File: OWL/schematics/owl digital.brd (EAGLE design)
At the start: 60 x 56.3 mm, 59 parts, among them IC1 REG1117, IC3 IS61WV51216BLL-10TLI, U2 WM8731, U4 STM32F405ZGT6

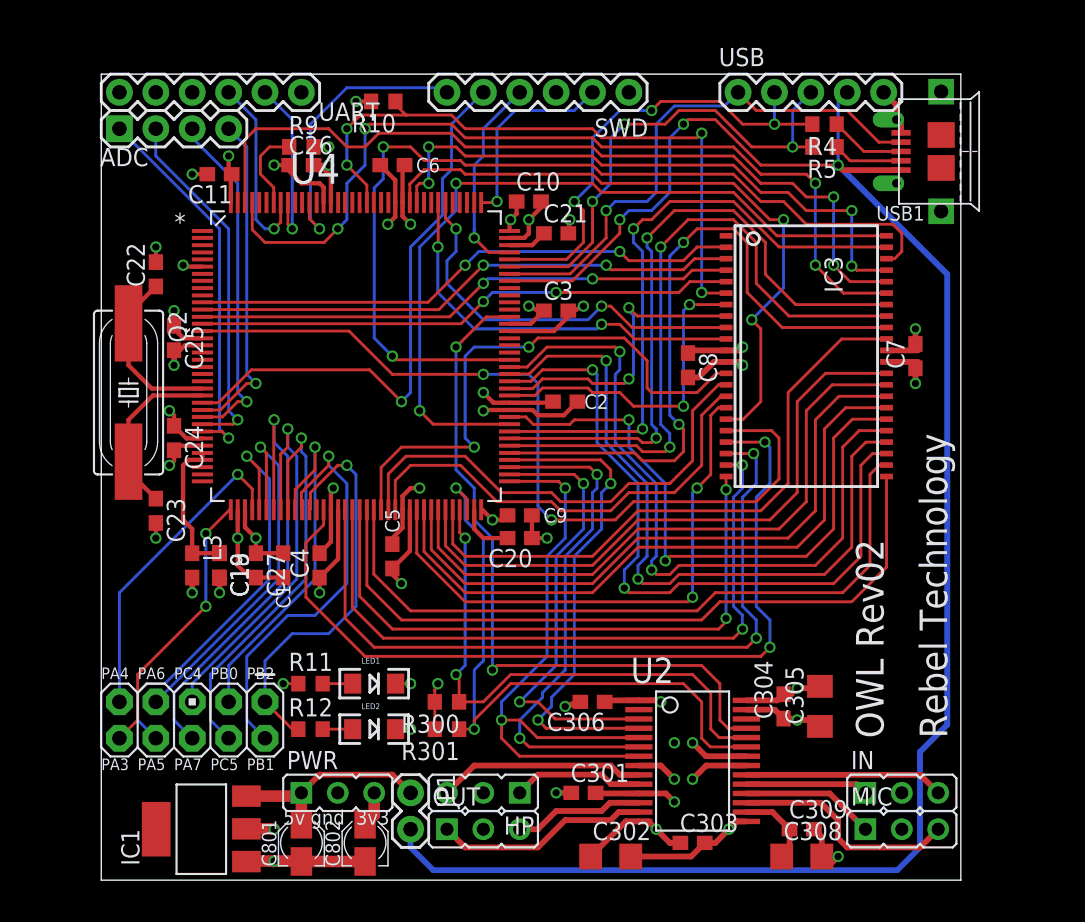
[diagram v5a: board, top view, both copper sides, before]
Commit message: updated usb connector
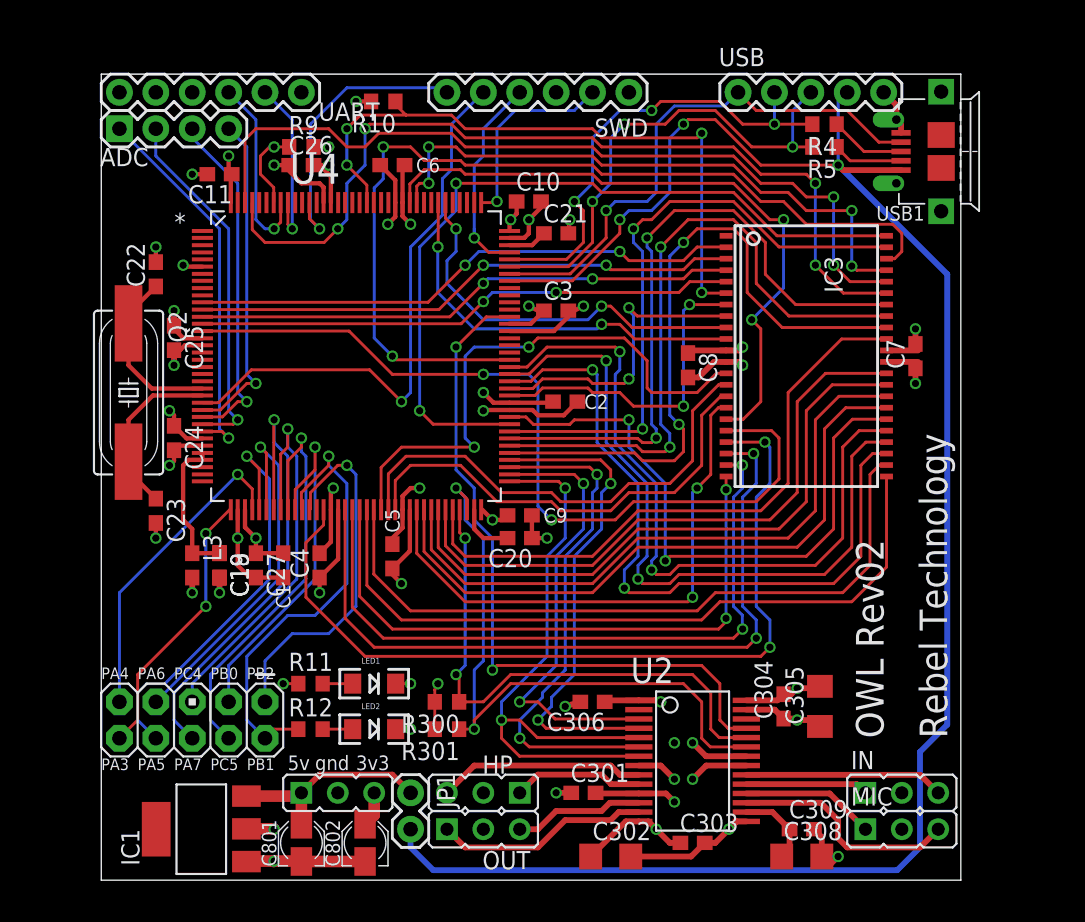
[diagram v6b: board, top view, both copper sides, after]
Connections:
- net PB1: now also R12.1
- net PB2: no longer R12.1
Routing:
- net PB2: track 28.6 -> 25.4 mm
- net PB1: track 29.3 -> 31.9 mm
- net BOOT0: vias 0 -> 1
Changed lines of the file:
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@@
 <text x="10.16" y="14.2875" size="0.8128" layer="21" font="vector" rot="SR0">PB2</text>
 <text x="54.61" y="10.16" size="1.9304" layer="21" font="vector" rot="R90">OWL Rev02</text>
-<text x="12.7" y="4.1275" size="1.016" layer="21" font="vector" rot="SR0">5v</text>
-<text x="14.605" y="4.1275" size="1.016" layer="21" font="vector" rot="SR0">gnd</text>
-<text x="17.78" y="4.1275" size="1.016" layer="21" font="vector" rot="SR0">3v3</text>
+<text x="13.0175" y="7.9375" size="1.016" layer="21" font="vector" rot="SR0">5v</text>
+<text x="14.9225" y="7.9375" size="1.016" layer="21" font="vector" rot="SR0">gnd</text>
+<text x="17.78" y="7.9375" size="1.016" layer="21" font="vector" rot="SR0">3v3</text>
 <dimension x1="0" y1="0.254" x2="0" y2="56.515" x3="-3.175" y3="28.3845" textsize="1.778" textratio="2" layer="51" width="0.1" visible="yes"/>
 </plain>
@@
 </class>
 </classes>
-<designrules name="Rebel">
+<designrules name="Rebel *">
 <description language="de">
 &lt;b&gt;Rebel Rules&lt;/b&gt;
@@
 <param name="checkAngle" value="0"/>
 <param name="checkFont" value="1"/>
-<param name="checkRestrict" value="0"/>
+<param name="checkRestrict" value="1"/>
 <param name="useDiameter" value="13"/>
 <param name="maxErrors" value="50"/>
@@
 <element name="C302" library="resistor" package="C1206" value="10u" x="35.56" y="1.905"/>
 <element name="C301" library="resistor" package="C0603" value="100n" x="33.655" y="6.35"/>
-<element name="HP" library="audioint" package="JMP/3P/SIP" value="" x="26.67" y="6.35" rot="R180"/>
+<element name="HP" library="audioint" package="JMP/3P/SIP" value="" x="26.67" y="6.35" smashed="yes" rot="R180">
+<attribute name="NAME" x="26.6065" y="7.6835" size="1.27" layer="25" ratio="10"/>
+<attribute name="VALUE" x="30.226" y="9.398" size="1.27" layer="27" ratio="10" rot="R180"/>
+</element>
 <element name="R300" library="resistor" package="R0603" value="4k7" x="24.13" y="12.7" rot="R180"/>
 <element name="R301" library="resistor" package="R0603" value="4k7" x="24.13" y="10.795" rot="R180"/>
 <element name="IN" library="audioint" package="JMP/3P/SIP" value="" x="55.88" y="6.35"/>
-<element name="OUT" library="audioint" package="JMP/3P/SIP" value="" x="26.67" y="3.81"/>
+<element name="OUT" library="audioint" package="JMP/3P/SIP" value="" x="26.67" y="3.81" smashed="yes">
+<attribute name="NAME" x="26.6065" y="1.016" size="1.27" layer="25" ratio="10"/>
+<attribute name="VALUE" x="23.114" y="0.762" size="1.27" layer="27" ratio="10"/>
+</element>
 <element name="USB" library="SparkFun" package="1X05" value="" x="44.45" y="55.245"/>
 <element name="ADC" library="SparkFun" package="1X04" value="" x="1.27" y="52.705" smashed="yes">
@@
 <attribute name="VALUE" x="0" y="49.53" size="1.27" layer="27"/>
 </element>
-<element name="PWR" library="audioint" package="JMP/3P/SIP" value="" x="16.51" y="6.35"/>
+<element name="PWR" library="audioint" package="JMP/3P/SIP" value="" x="16.51" y="6.35" smashed="yes">
+<attribute name="VALUE" x="12.954" y="3.302" size="1.27" layer="27" ratio="10"/>
+</element>
 <element name="USB1" library="USB_connector" package="HRS_ZX62D-AB-5P8_USB" value="" x="58.7375" y="51.1175" rot="R90"/>
 </elements>
@@
 <wire x1="15.875" y1="29.21" x2="15.875" y2="29.845" width="0.2032" layer="1"/>
 <wire x1="17.145" y1="27.94" x2="15.875" y2="29.21" width="0.2032" layer="16"/>
+<contactref element="R12" pad="1"/>
+<wire x1="13.755" y1="10.795" x2="12.065" y2="10.795" width="0.2032" layer="1"/>
+<wire x1="12.065" y1="10.795" x2="11.43" y2="10.16" width="0.2032" layer="1"/>
 </signal>
 <signal name="PB2">
 <contactref element="JP2" pad="1"/>
-<contactref element="R12" pad="1"/>
 <contactref element="U4" pad="48"/>
 <wire x1="14.5288" y1="26.1112" x2="14.605" y2="26.1874" width="0.2032" layer="1"/>
@@
 <wire x1="14.605" y1="27.305" x2="16.51" y2="29.21" width="0.2032" layer="1"/>
 <wire x1="16.51" y1="29.21" x2="17.145" y2="29.21" width="0.2032" layer="1"/>
-<wire x1="13.755" y1="10.795" x2="13.335" y2="10.795" width="0.2032" layer="1"/>
-<wire x1="13.335" y1="10.795" x2="11.43" y2="12.7" width="0.2032" layer="1"/>
 <wire x1="17.78" y1="28.575" x2="17.145" y2="29.21" width="0.2032" layer="16"/>
 </signal>
@@
 <wire x1="11.1125" y1="49.53" x2="11.1125" y2="50.8" width="0.2032" layer="1"/>
 <wire x1="11.1125" y1="50.8" x2="11.7475" y2="51.435" width="0.2032" layer="1"/>
-<wire x1="11.7475" y1="51.435" x2="13.12" y2="51.435" width="0.2032" layer="1"/>
+<wire x1="11.7475" y1="51.435" x2="12.065" y2="51.435" width="0.2032" layer="1"/>
+<via x="12.065" y="51.435" extent="1-16" drill="0.5" shape="square"/>
+<wire x1="12.065" y1="51.435" x2="13.12" y2="51.435" width="0.2032" layer="1"/>
 </signal>
 <signal name="ADC2">
